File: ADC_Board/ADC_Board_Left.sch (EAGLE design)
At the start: 24 parts

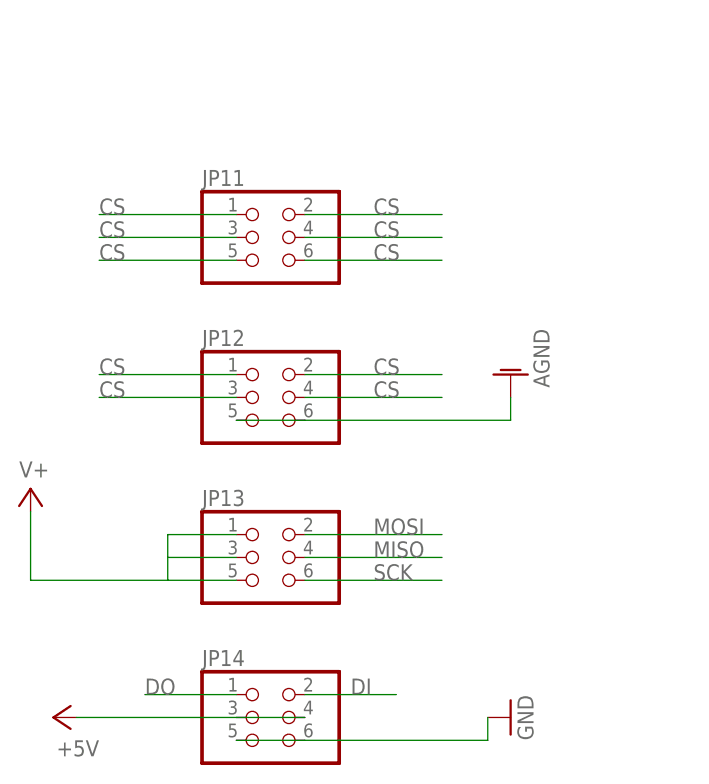
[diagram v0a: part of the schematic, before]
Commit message: Alterações ligeiras nos esquemas eléctricos das placas das ADCs.
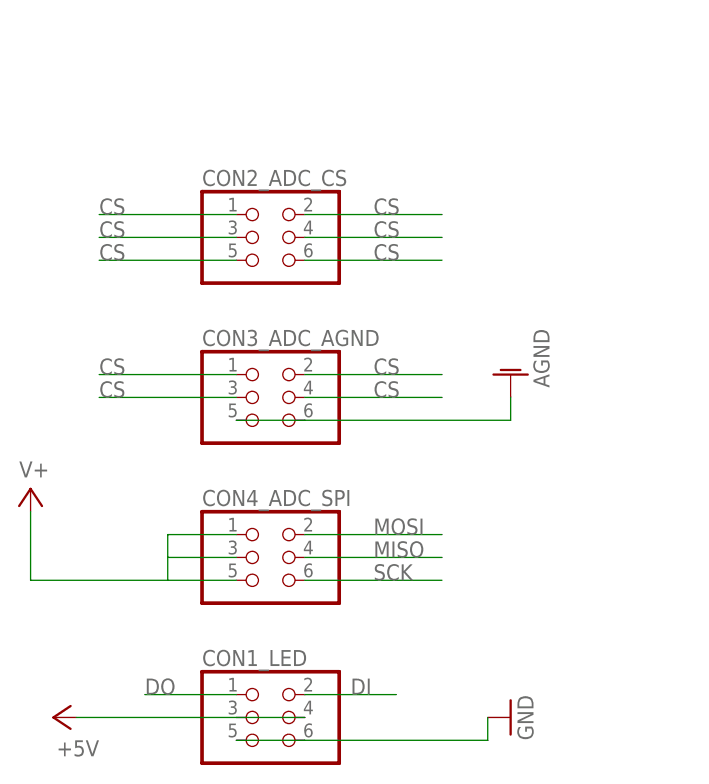
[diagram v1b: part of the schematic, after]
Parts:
- renumbered JP11 to CON2_ADC_CS, JP12 to CON3_ADC_AGND, JP13 to CON4_ADC_SPI, JP14 to CON1_LED
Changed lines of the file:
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@@
 <part name="JP9" library="pinhead" deviceset="PINHD-1X6" device=""/>
 <part name="JP10" library="pinhead" deviceset="PINHD-1X6" device=""/>
-<part name="JP11" library="pinhead" deviceset="PINHD-2X3" device=""/>
-<part name="JP12" library="pinhead" deviceset="PINHD-2X3" device=""/>
+<part name="CON2_ADC_CS" library="pinhead" deviceset="PINHD-2X3" device=""/>
+<part name="CON3_ADC_AGND" library="pinhead" deviceset="PINHD-2X3" device=""/>
 <part name="AGND1" library="supply1" deviceset="AGND" device=""/>
-<part name="JP13" library="pinhead" deviceset="PINHD-2X3" device=""/>
-<part name="JP14" library="pinhead" deviceset="PINHD-2X3" device=""/>
+<part name="CON4_ADC_SPI" library="pinhead" deviceset="PINHD-2X3" device=""/>
+<part name="CON1_LED" library="pinhead" deviceset="PINHD-2X3" device=""/>
 <part name="P+3" library="supply1" deviceset="+5V" device=""/>
 <part name="GND3" library="supply1" deviceset="GND" device=""/>
@@
 <instance part="JP9" gate="A" x="-15.24" y="111.76"/>
 <instance part="JP10" gate="A" x="-5.08" y="111.76"/>
-<instance part="JP11" gate="A" x="-78.74" y="58.42"/>
-<instance part="JP12" gate="A" x="-78.74" y="40.64"/>
+<instance part="CON2_ADC_CS" gate="A" x="-78.74" y="58.42"/>
+<instance part="CON3_ADC_AGND" gate="A" x="-78.74" y="40.64"/>
 <instance part="AGND1" gate="VR1" x="-50.8" y="43.18" rot="R180"/>
-<instance part="JP13" gate="A" x="-78.74" y="22.86"/>
-<instance part="JP14" gate="A" x="-78.74" y="5.08"/>
+<instance part="CON4_ADC_SPI" gate="A" x="-78.74" y="22.86"/>
+<instance part="CON1_LED" gate="A" x="-78.74" y="5.08"/>
 <instance part="P+3" gate="1" x="-101.6" y="5.08" rot="R90"/>
 <instance part="GND3" gate="1" x="-50.8" y="5.08" rot="R90"/>
@@
 <net name="GND" class="0">
 <segment>
-<pinref part="JP14" gate="A" pin="5"/>
-<pinref part="JP14" gate="A" pin="6"/>
+<pinref part="CON1_LED" gate="A" pin="5"/>
+<pinref part="CON1_LED" gate="A" pin="6"/>
 <wire x1="-81.28" y1="2.54" x2="-73.66" y2="2.54" width="0.1524" layer="91"/>
 <pinref part="GND3" gate="1" pin="GND"/>
@@
 </segment>
 <segment>
-<pinref part="JP14" gate="A" pin="3"/>
+<pinref part="CON1_LED" gate="A" pin="3"/>
 <pinref part="P+3" gate="1" pin="+5V"/>
 <wire x1="-99.06" y1="5.08" x2="-81.28" y2="5.08" width="0.1524" layer="91"/>
-<pinref part="JP14" gate="A" pin="4"/>
+<pinref part="CON1_LED" gate="A" pin="4"/>
 <wire x1="-81.28" y1="5.08" x2="-73.66" y2="5.08" width="0.1524" layer="91"/>
 </segment>
@@
 <segment>
 <wire x1="-73.66" y1="25.4" x2="-58.42" y2="25.4" width="0.1524" layer="91"/>
-<pinref part="JP13" gate="A" pin="2"/>
+<pinref part="CON4_ADC_SPI" gate="A" pin="2"/>
 <label x="-66.04" y="25.4" size="1.778" layer="95"/>
 </segment>
@@
 <wire x1="-73.66" y1="20.32" x2="-58.42" y2="20.32" width="0.1524" layer="91"/>
 <label x="-66.04" y="20.32" size="1.778" layer="95"/>
-<pinref part="JP13" gate="A" pin="6"/>
+<pinref part="CON4_ADC_SPI" gate="A" pin="6"/>
 </segment>
 </net>
@@
 <segment>
 <wire x1="-73.66" y1="22.86" x2="-58.42" y2="22.86" width="0.1524" layer="91"/>
-<pinref part="JP13" gate="A" pin="4"/>
+<pinref part="CON4_ADC_SPI" gate="A" pin="4"/>
 <label x="-66.04" y="22.86" size="1.778" layer="95"/>
 </segment>
@@
 </segment>
 <segment>
-<pinref part="JP13" gate="A" pin="5"/>
+<pinref part="CON4_ADC_SPI" gate="A" pin="5"/>
 <pinref part="SUPPLY4" gate="1" pin="V+"/>
 <wire x1="-81.28" y1="20.32" x2="-88.9" y2="20.32" width="0.1524" layer="91"/>
 <wire x1="-88.9" y1="20.32" x2="-104.14" y2="20.32" width="0.1524" layer="91"/>
 <wire x1="-104.14" y1="20.32" x2="-104.14" y2="27.94" width="0.1524" layer="91"/>
-<pinref part="JP13" gate="A" pin="3"/>
+<pinref part="CON4_ADC_SPI" gate="A" pin="3"/>
 <wire x1="-81.28" y1="22.86" x2="-88.9" y2="22.86" width="0.1524" layer="91"/>
 <wire x1="-88.9" y1="22.86" x2="-88.9" y2="20.32" width="0.1524" layer="91"/>
-<pinref part="JP13" gate="A" pin="1"/>
+<pinref part="CON4_ADC_SPI" gate="A" pin="1"/>
 <wire x1="-81.28" y1="25.4" x2="-88.9" y2="25.4" width="0.1524" layer="91"/>
 <wire x1="-88.9" y1="25.4" x2="-88.9" y2="22.86" width="0.1524" layer="91"/>
@@
 </segment>
 <segment>
-<pinref part="JP12" gate="A" pin="6"/>
+<pinref part="CON3_ADC_AGND" gate="A" pin="6"/>
 <pinref part="AGND1" gate="VR1" pin="AGND"/>
 <wire x1="-73.66" y1="38.1" x2="-50.8" y2="38.1" width="0.1524" layer="91"/>
 <wire x1="-50.8" y1="38.1" x2="-50.8" y2="40.64" width="0.1524" layer="91"/>
-<pinref part="JP12" gate="A" pin="5"/>
+<pinref part="CON3_ADC_AGND" gate="A" pin="5"/>
 <wire x1="-73.66" y1="38.1" x2="-81.28" y2="38.1" width="0.1524" layer="91"/>
 </segment>
@@
 <label x="-91.44" y="7.62" size="1.778" layer="95"/>
 <wire x1="-81.28" y1="7.62" x2="-91.44" y2="7.62" width="0.1524" layer="91"/>
-<pinref part="JP14" gate="A" pin="1"/>
+<pinref part="CON1_LED" gate="A" pin="1"/>
 </segment>
 <segment>
@@
 <label x="-68.58" y="7.62" size="1.778" layer="95"/>
 <wire x1="-73.66" y1="7.62" x2="-63.5" y2="7.62" width="0.1524" layer="91"/>
-<pinref part="JP14" gate="A" pin="2"/>
+<pinref part="CON1_LED" gate="A" pin="2"/>
 </segment>
 <segment>
@@
 <segment>
 <wire x1="-81.28" y1="60.96" x2="-96.52" y2="60.96" width="0.1524" layer="91"/>
-<pinref part="JP11" gate="A" pin="1"/>
+<pinref part="CON2_ADC_CS" gate="A" pin="1"/>
 <label x="-96.52" y="60.96" size="1.778" layer="95"/>
 </segment>
 <segment>
 <wire x1="-81.28" y1="58.42" x2="-96.52" y2="58.42" width="0.1524" layer="91"/>
-<pinref part="JP11" gate="A" pin="3"/>
+<pinref part="CON2_ADC_CS" gate="A" pin="3"/>
 <label x="-96.52" y="58.42" size="1.778" layer="95"/>
 </segment>
 <segment>
 <wire x1="-81.28" y1="55.88" x2="-96.52" y2="55.88" width="0.1524" layer="91"/>
-<pinref part="JP11" gate="A" pin="5"/>
+<pinref part="CON2_ADC_CS" gate="A" pin="5"/>
 <label x="-96.52" y="55.88" size="1.778" layer="95"/>
 </segment>
 <segment>
 <wire x1="-58.42" y1="60.96" x2="-73.66" y2="60.96" width="0.1524" layer="91"/>
-<pinref part="JP11" gate="A" pin="2"/>
+<pinref part="CON2_ADC_CS" gate="A" pin="2"/>
 <label x="-66.04" y="60.96" size="1.778" layer="95"/>
 </segment>
 <segment>
 <wire x1="-58.42" y1="58.42" x2="-73.66" y2="58.42" width="0.1524" layer="91"/>
-<pinref part="JP11" gate="A" pin="4"/>
+<pinref part="CON2_ADC_CS" gate="A" pin="4"/>
 <label x="-66.04" y="58.42" size="1.778" layer="95"/>
 </segment>
 <segment>
 <wire x1="-58.42" y1="55.88" x2="-73.66" y2="55.88" width="0.1524" layer="91"/>
-<pinref part="JP11" gate="A" pin="6"/>
+<pinref part="CON2_ADC_CS" gate="A" pin="6"/>
 <label x="-66.04" y="55.88" size="1.778" layer="95"/>
 </segment>
 <segment>
 <wire x1="-81.28" y1="43.18" x2="-96.52" y2="43.18" width="0.1524" layer="91"/>
-<pinref part="JP12" gate="A" pin="1"/>
+<pinref part="CON3_ADC_AGND" gate="A" pin="1"/>
 <label x="-96.52" y="43.18" size="1.778" layer="95"/>
 </segment>
 <segment>
 <wire x1="-81.28" y1="40.64" x2="-96.52" y2="40.64" width="0.1524" layer="91"/>
-<pinref part="JP12" gate="A" pin="3"/>
+<pinref part="CON3_ADC_AGND" gate="A" pin="3"/>
 <label x="-96.52" y="40.64" size="1.778" layer="95"/>
 </segment>
 <segment>
 <wire x1="-73.66" y1="43.18" x2="-58.42" y2="43.18" width="0.1524" layer="91"/>
-<pinref part="JP12" gate="A" pin="2"/>
+<pinref part="CON3_ADC_AGND" gate="A" pin="2"/>
 <label x="-66.04" y="43.18" size="1.778" layer="95"/>
 </segment>
 <segment>
 <wire x1="-73.66" y1="40.64" x2="-58.42" y2="40.64" width="0.1524" layer="91"/>
-<pinref part="JP12" gate="A" pin="4"/>
+<pinref part="CON3_ADC_AGND" gate="A" pin="4"/>
 <label x="-66.04" y="40.64" size="1.778" layer="95"/>
 </segment>
